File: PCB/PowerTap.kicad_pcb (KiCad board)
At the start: 2 copper layers, 23 x 23 mm, 4 parts, among them CON1 BARREL_JACK

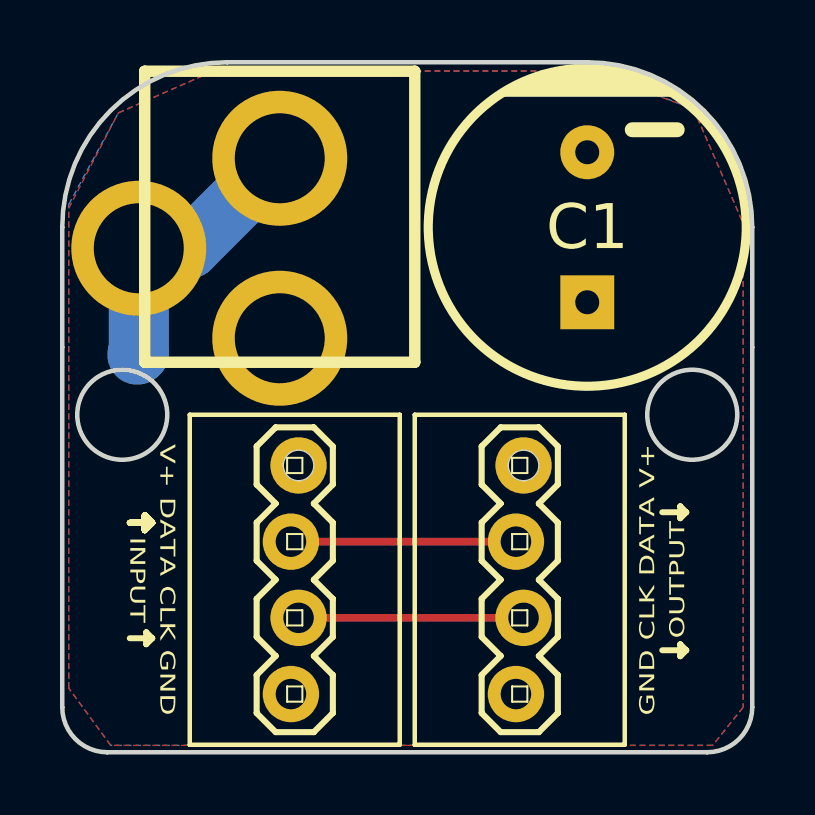
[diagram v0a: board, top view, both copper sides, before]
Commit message: More Changes to AllPixel and PowerTap for DFM
AP: added silk labels for components
AP: minor trace tweak on USB data pin to avoid right angle
PT: fixed ground trace too long
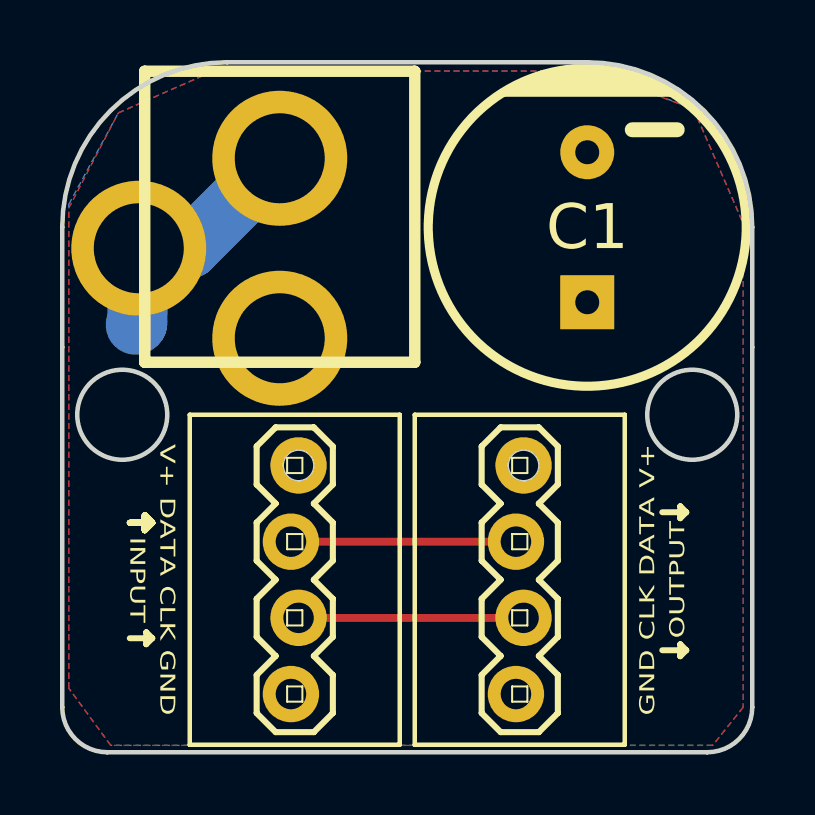
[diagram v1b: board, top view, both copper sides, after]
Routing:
- net GND: track 9.51 -> 8.51 mm
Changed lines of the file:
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@@
   (page A3)
   (layers
-    (15 F.Cu signal)
-    (0 B.Cu signal hide)
+    (15 F.Cu signal hide)
+    (0 B.Cu signal)
     (16 B.Adhes user)
     (17 F.Adhes user)
@@
   (gr_line (start 110.5 50) (end 98.5 50) (angle 90) (layer Edge.Cuts) (width 0.15))
   (gr_line (start 116 55.5) (end 116 59.5) (angle 90) (layer Edge.Cuts) (width 0.15))
-  (segment (start 95.551 56.2004) (end 95.551 59.699) (width 2) (layer B.Cu) (net 1))
-  (segment (start 95.551 59.699) (end 95.5 59.75) (width 2) (layer B.Cu) (net 1))
+  (segment (start 95.551 56.2004) (end 95.5 58.7) (width 2) (layer B.Cu) (net 1) (status 400000))
+  (segment (start 95.5 58.7) (end 95.449 58.751) (width 2) (layer B.Cu) (net 1))
   (segment (start 95.551 56.2004) (end 97.25026 56.2004) (width 2) (layer B.Cu) (net 1))
   (segment (start 97.25026 56.2004) (end 100.25 53.20066) (width 2) (layer B.Cu) (net 1))
